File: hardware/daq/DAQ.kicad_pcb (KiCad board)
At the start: 2 copper layers, 99 x 99 mm, 142 parts, among them J1 ICD15S13E4GX00LF, J2 ICD15S13E4GX00LF, J3 ICD15S13E4GX00LF, P1 0022272021, U1 ADS124S08IRHBT, U2 ADS124S08IRHBT, U3 LT6654BMPS6-5-TRMPBF, U4 LM1086IS-5.0_NOPB, U5 TPS73801DCQR, U6 TPSM63603RDHR, U7 TPSM63603RDHR, U8 TPSM63603RDHR

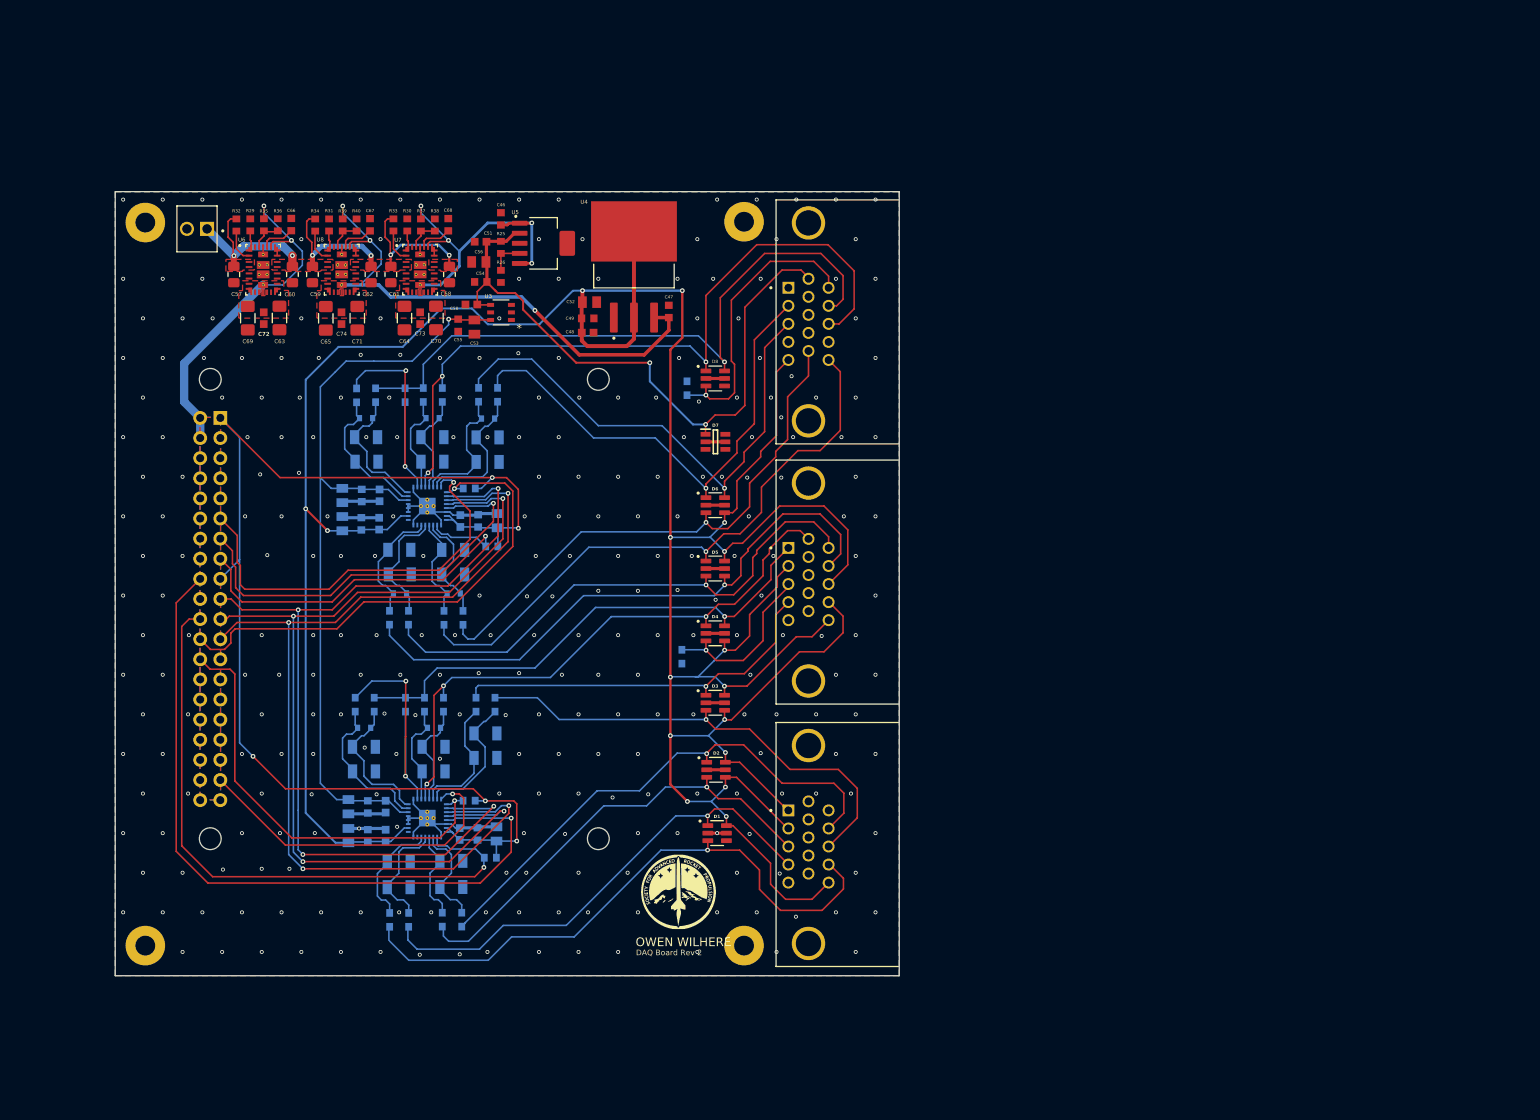
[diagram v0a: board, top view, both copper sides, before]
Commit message: added an ADC to schematic and started absolutely destroying the layout
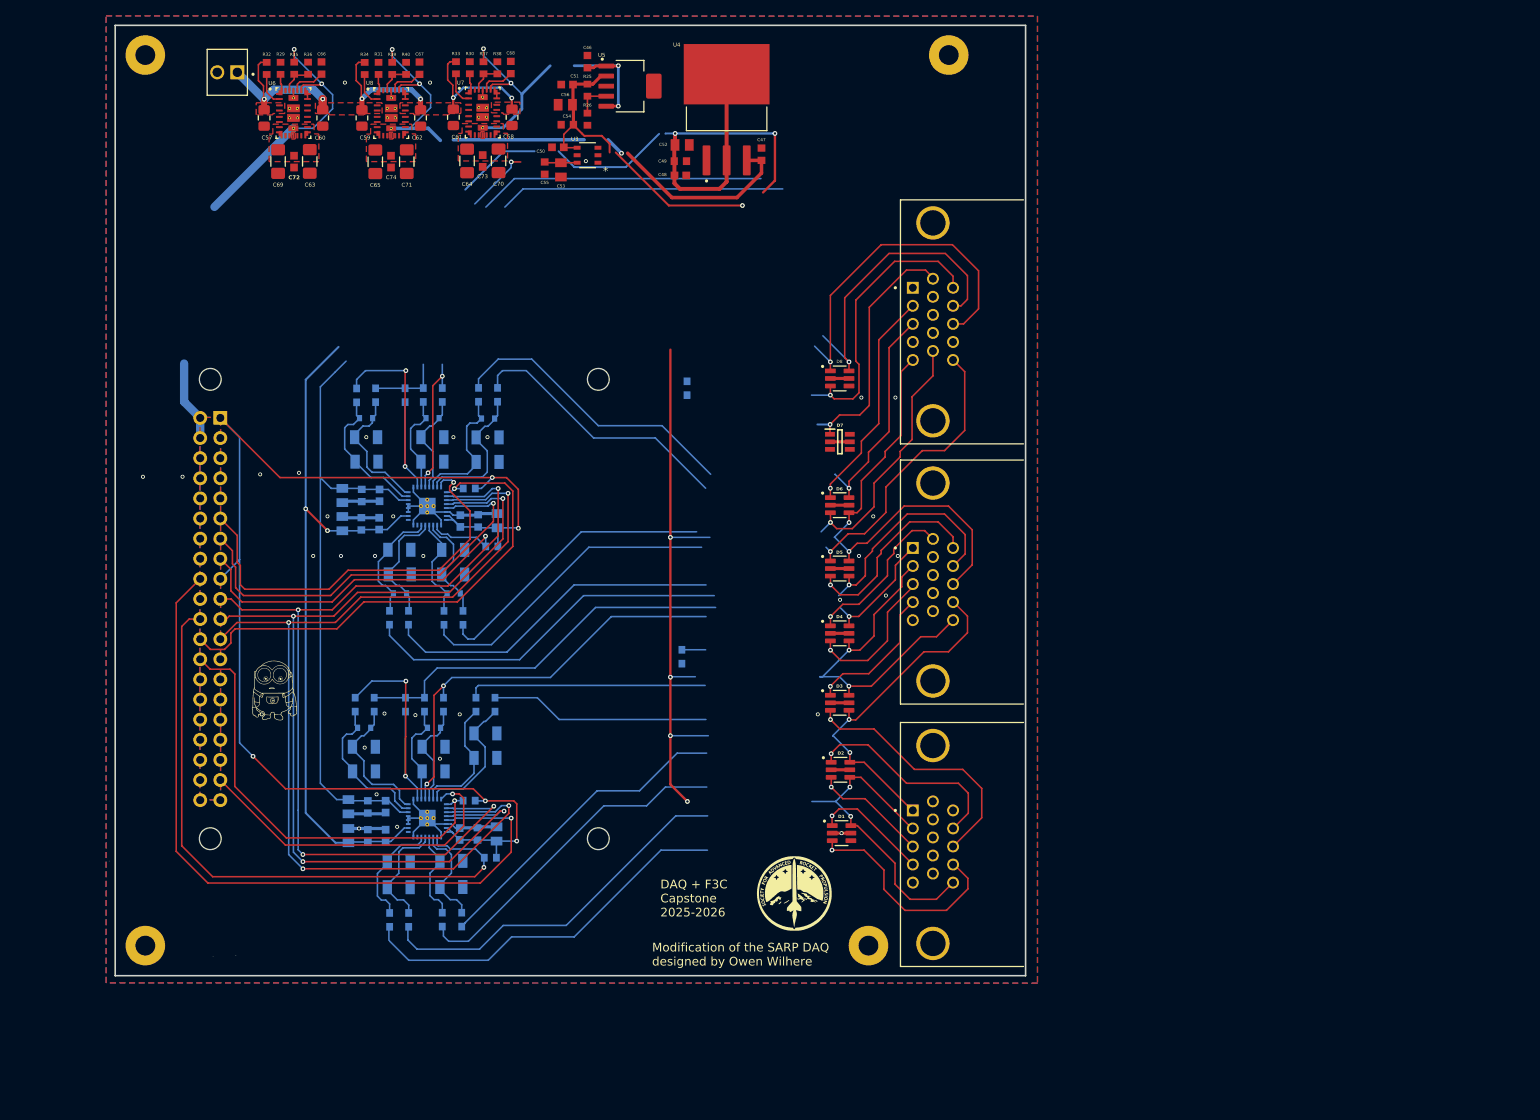
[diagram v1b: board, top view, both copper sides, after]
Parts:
- added G***: LOGO, LOGO, F.Cu at (100.1, 102.8)
- added G***: LOGO, LOGO, F.Cu at (85.5, 128.2)
- moved H1 33.3 mm to (185.2, 22.8)
- moved C47 23.0 mm to (161.6, 35.3)
- moved C49 23.0 mm to (151.4, 36.1)
- moved C52 23.0 mm to (151.6, 34.1)
- moved U4 23.0 mm to (157.2, 29.6)
- moved C48 23.0 mm to (151.4, 38.0)
- moved C46 22.7 mm to (139.6, 23.6)
- moved C51 22.7 mm to (137.1, 26.5)
- moved R26 22.7 mm to (139.6, 30.9)
- moved R25 22.7 mm to (139.6, 27.2)
- moved U5 22.7 mm to (145.0, 26.7)
- moved C53 22.7 mm to (136.3, 37.2)
- moved C50 22.7 mm to (135.9, 34.4)
- moved C54 22.7 mm to (137.1, 31.6)
- moved C55 22.7 mm to (134.2, 37.0)
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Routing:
- net 10Vs: track 81.7 -> 71.7 mm
- net 5V REF: track 100.3 -> 91.9 mm
- net +5Vs: track 429.2 -> 421.1 mm
- net /IDAC2_1: track 94.0 -> 97.8 mm
- net GND: vias 288 -> 34
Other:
- board size 99 x 99 mm -> 114.9 x 120 mm
- board text added: "DAQ + F3C Capstone 2025-2026"
- board text added: "Modification of the SARP DAQ designed by Owen Wilhere"
- board text removed: "DAQ Board Rev 2"
- board text removed: "OWEN WILHERE"

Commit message: last commit before I replace the 15-pin DSUBs with 26-pin
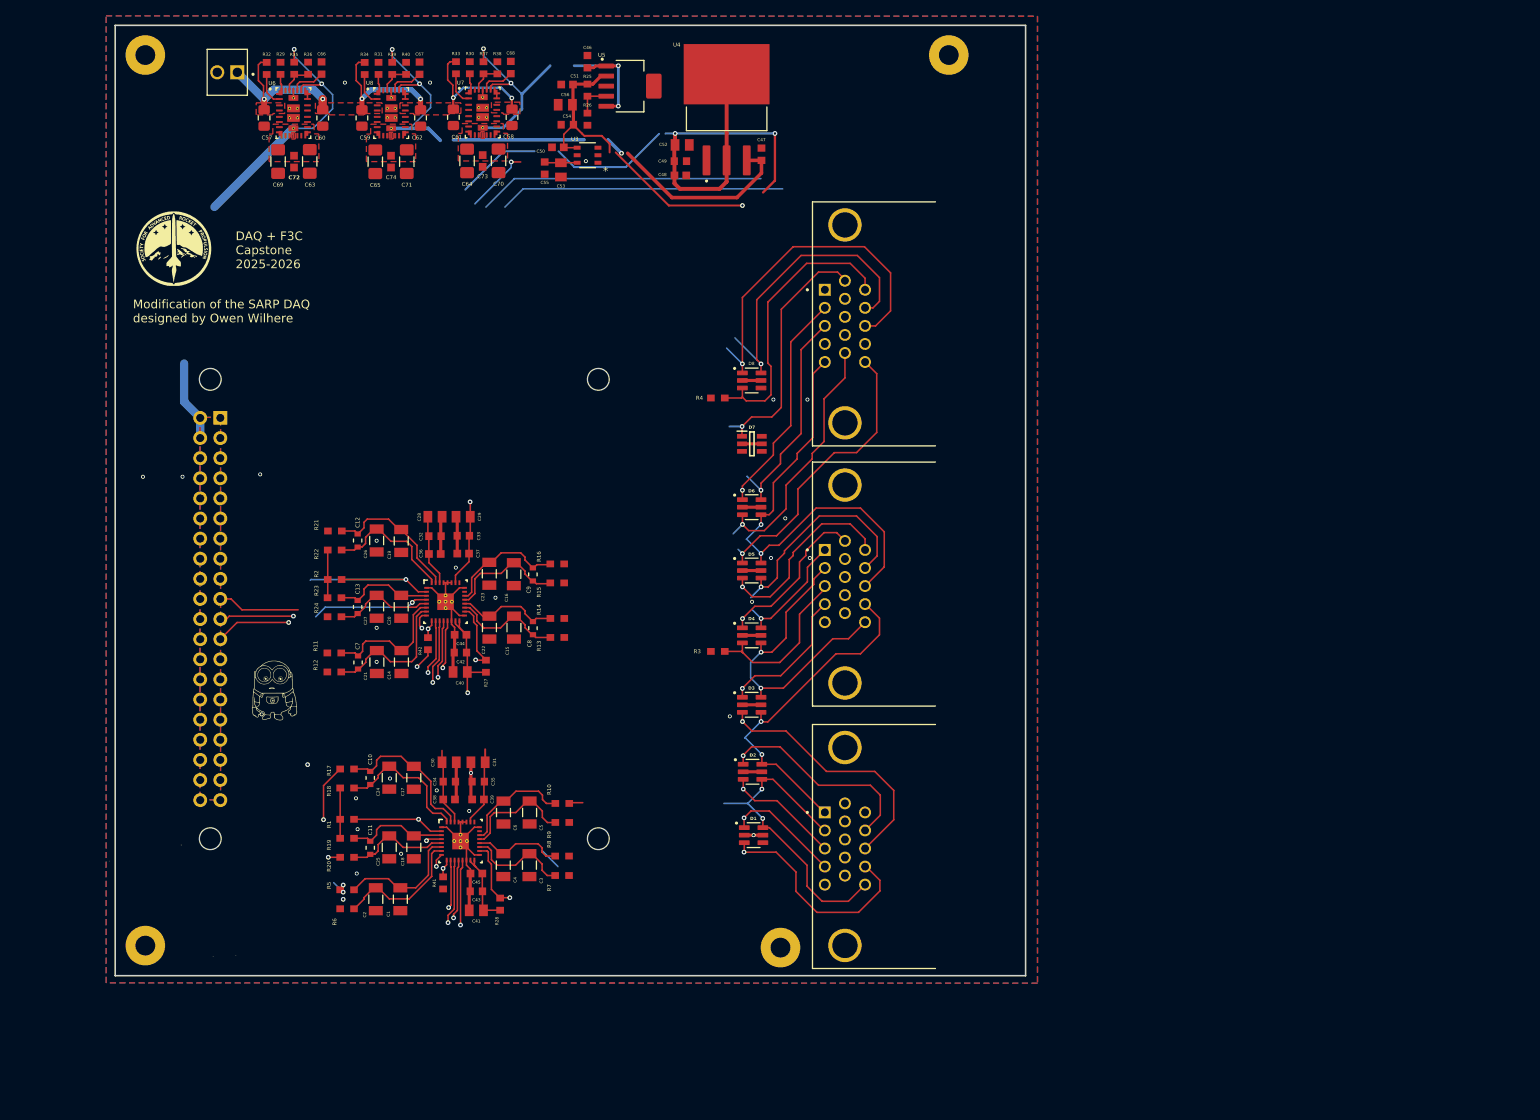
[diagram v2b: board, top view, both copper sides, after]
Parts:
- C1, C10, C11, C12, C13, C14, C15, C16, C17, C18, C19, C2, C20, C21, C22, C23, C24, C25, C26, C27, C28, C29, C3, C30, C31, C32, C33, C34, C35, C36, C37, C38, C39, C4, C40, C41, C42, C43, C44, C45, C5, C6, C7, C8, C9, R1, R10, R11, R12, R13, R14, R15, R16, R17, R18, R19, R2, R20, R21, R22, R23, R24, R27, R28, R3, R4, R41, R42, R5, R6, R7, R8, R9, U1, U2: moved to F.Cu
- moved G*** 113.0 mm to (88.1, 47.1)
- moved R12 40.6 mm to (107.7, 100.7), turned to 0 degrees
- moved R11 37.3 mm to (107.7, 98.2), turned to 0 degrees
- moved C7 34.9 mm to (110.7, 99.5), turned to -90 degrees
- moved R6 31.8 mm to (109.3, 130.6), turned to 0 degrees
- moved C21 31.6 mm to (113.0, 99.4), turned to -90 degrees
- moved R24 31.1 mm to (107.7, 93.7), turned to 180 degrees
- moved R5 28.5 mm to (109.3, 128.2), turned to 0 degrees
- moved R23 27.9 mm to (107.7, 91.3), turned to 180 degrees
- moved C14 27.5 mm to (116.1, 99.4), turned to -90 degrees
- moved R10 26.3 mm to (136.5, 117.3), turned to 180 degrees
- moved C13 25.7 mm to (110.6, 92.4), turned to -90 degrees
- moved C2 25.1 mm to (112.9, 129.3), turned to -90 degrees
- moved R2 24.9 mm to (107.7, 89.0), turned to 180 degrees
- moved R9 23.0 mm to (136.5, 119.7), turned to 180 degrees
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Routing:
- net +5Vs: track 421.1 -> 276.8 mm, vias 16 -> 11
- net +3.3V: track 165.5 -> 27.0 mm, vias 5 -> 2
- net /SCLK: track 125.7 -> 25.9 mm
- net /MISO: track 119.5 -> 24.4 mm, vias 4 -> 3
- net /MOSI: track 116.4 -> 23.5 mm, vias 4 -> 3
- net /DRDY_N2: track 93.8 -> 8.30 mm
- net /RESET_N2: track 79.5 -> 8.85 mm
- net /CE1: track 63.6 -> 2.44 mm
- net 5V REF: track 91.9 -> 34.0 mm
- net /CE2: track 55.7 -> 2.31 mm
- net /IDAC2_2: track 74.1 -> 24.0 mm
- net /START_SYNC1: track 52.1 -> 2.40 mm
- net /LS3_SIG-: track 75.8 -> 28.5 mm
- net /PT5_SIG: track 61.6 -> 14.7 mm
- net /PT6_SIG: track 76.6 -> 29.7 mm
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
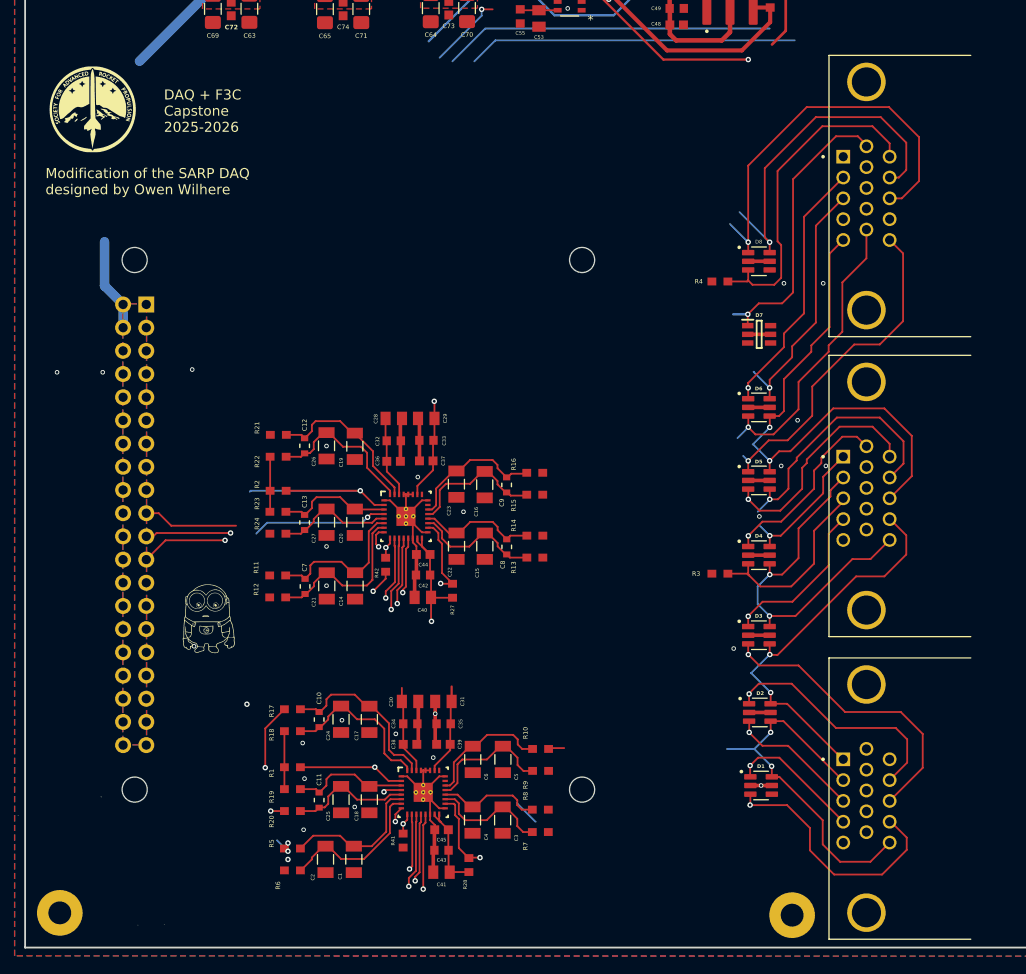
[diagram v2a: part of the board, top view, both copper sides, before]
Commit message: checking out 26pin, having footprint library issues yay
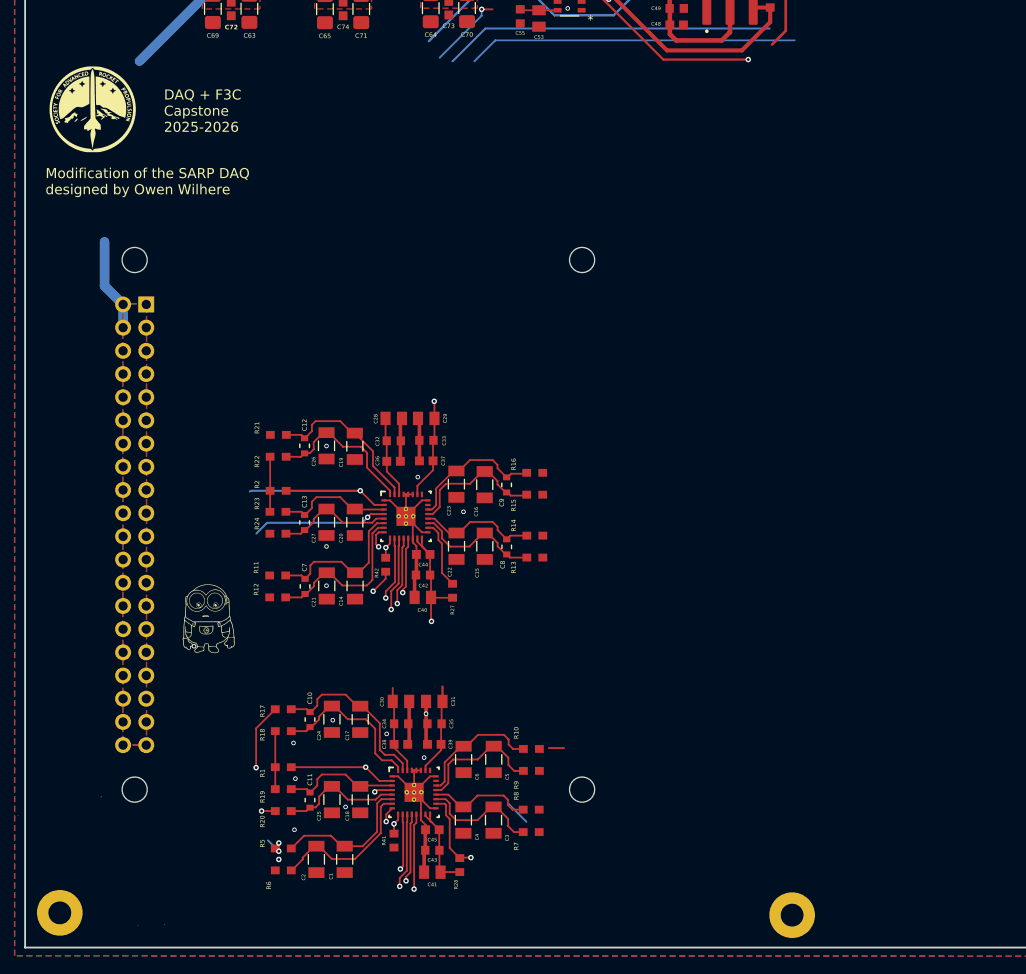
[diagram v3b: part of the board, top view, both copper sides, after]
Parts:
- removed D1, D2, D3, D4, D5, D6, D8: ESDA6V1BC6, ESDA6V1BC6:SOT95P280X145-6N
- removed D7: SMS12T1G, SMST12T1G:SOT95P275X110-6N
- removed J1, J2, J3: ICD15S13E4GX00LF, ICD15S13:AMPHENOL_ICD15S13E4GX00LF
- removed R3: 1.8k, footprints10kR:RC0603N_YAG-M
- removed R4: 1.8K, footprints10kR:RC0603N_YAG-M
- moved C1 1.00 mm to (115.0, 129.3)
- moved C10 1.00 mm to (111.2, 114.0)
- moved C11 1.00 mm to (111.2, 122.9)
- moved C17 1.00 mm to (116.7, 114.0)
- moved C18 1.00 mm to (116.7, 122.8)
- moved C2 1.00 mm to (111.9, 129.3)
- moved C24 1.00 mm to (113.6, 114.0)
- moved C25 1.00 mm to (113.6, 122.8)
- moved C3 1.00 mm to (131.3, 125.0)
- moved C30 1.00 mm to (121.2, 112.0)
- moved C31 1.00 mm to (124.8, 112.0)
- moved C34 1.00 mm to (121.2, 114.5)
- moved C35 1.00 mm to (124.8, 114.5)
- moved C38 1.00 mm to (121.2, 116.7)
- moved C39 1.00 mm to (124.8, 116.7)
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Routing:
- net +5Vs: track 276.8 -> 96.1 mm, vias 11 -> 3
- net /IDAC2_1: track 94.8 -> 50.9 mm, vias 2 -> 1
- net /RTD1_L1: track 80.5 -> 42.3 mm, vias 1 -> 0
- net /LS2_SIG-: track 36.6 -> 0.00 mm, vias 1 -> 0
- net /RTD1_L3: track 36.0 -> 0.00 mm
- net /PT2_SIG: track 32.8 -> 0.10 mm, vias 1 -> 0
- net /LS2_SIG+: track 32.6 -> 0.00 mm, vias 1 -> 0
- net 10Vs: track 71.7 -> 40.0 mm, vias 2 -> 1
- net /LS1_SIG-: track 28.6 -> 0.00 mm, vias 1 -> 0
- net /LS3_SIG-: track 28.5 -> 0.00 mm, vias 1 -> 0
- net /PT6_SIG: track 29.7 -> 1.69 mm, vias 1 -> 0
- net /LS1_SIG+: track 27.7 -> 0.00 mm, vias 1 -> 0
- net /PT3_SIG: track 26.7 -> 0.00 mm, vias 1 -> 0
- net /LS3_SIG+: track 24.7 -> 0.00 mm, vias 1 -> 0
- net /RTD2_L3: track 20.9 -> 0.00 mm
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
